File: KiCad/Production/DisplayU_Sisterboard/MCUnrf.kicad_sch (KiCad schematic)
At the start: 1 part, among them U1 nRF52820-CFAA-D-R7

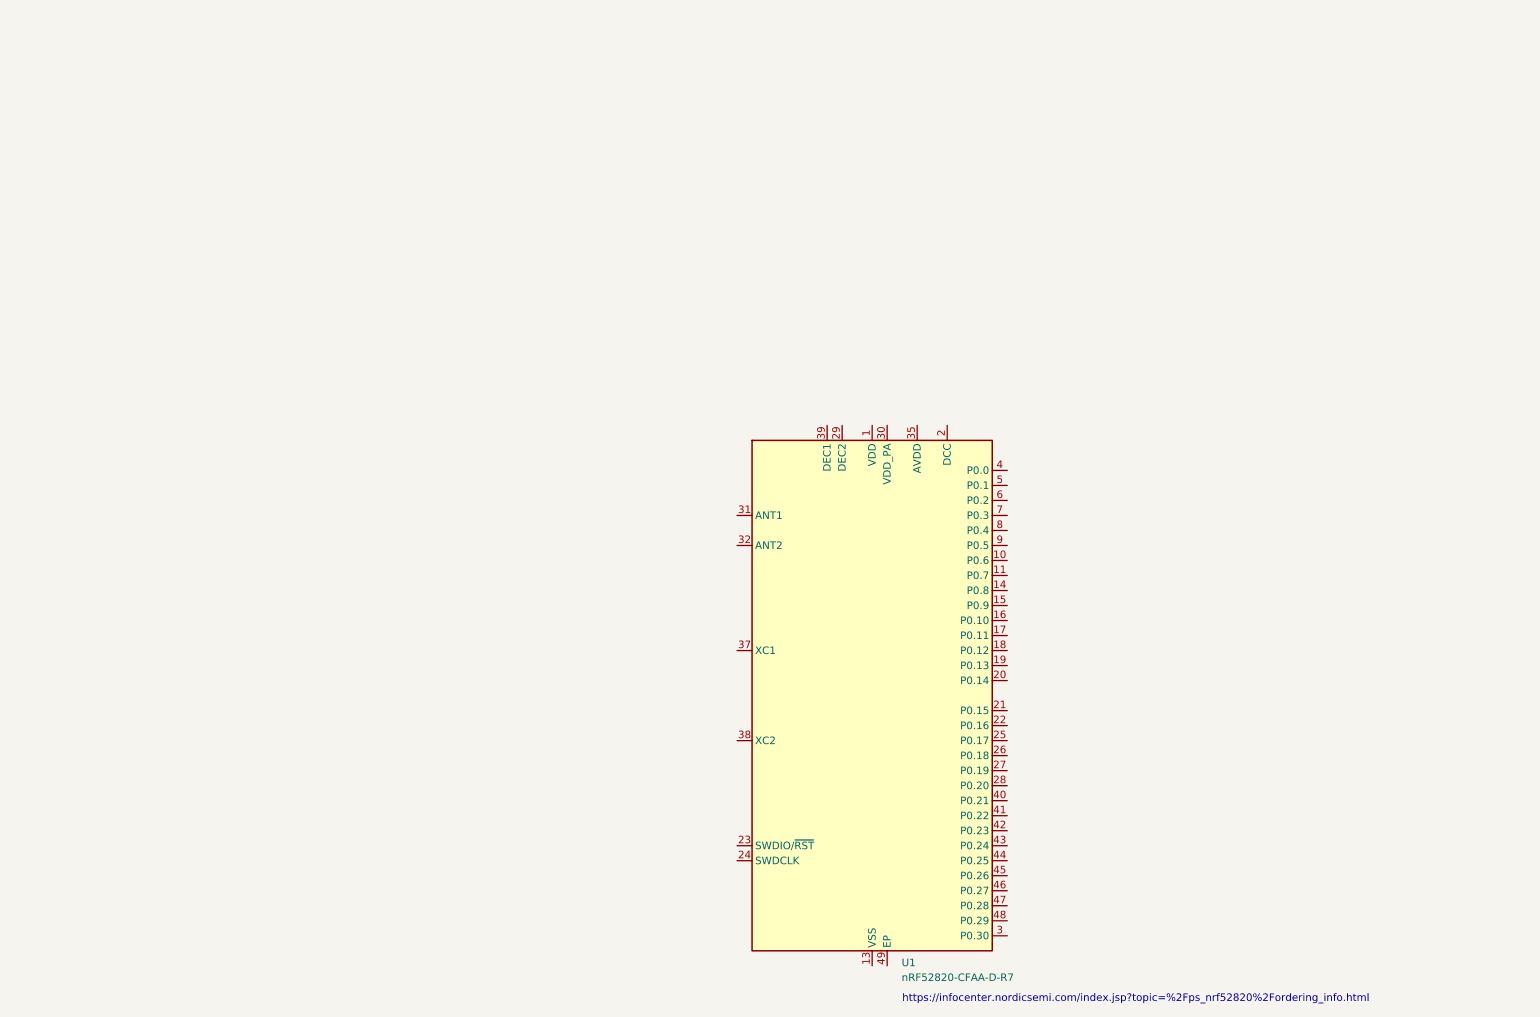
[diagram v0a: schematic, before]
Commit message: Microcontroller Choice
Nordic nRF52820
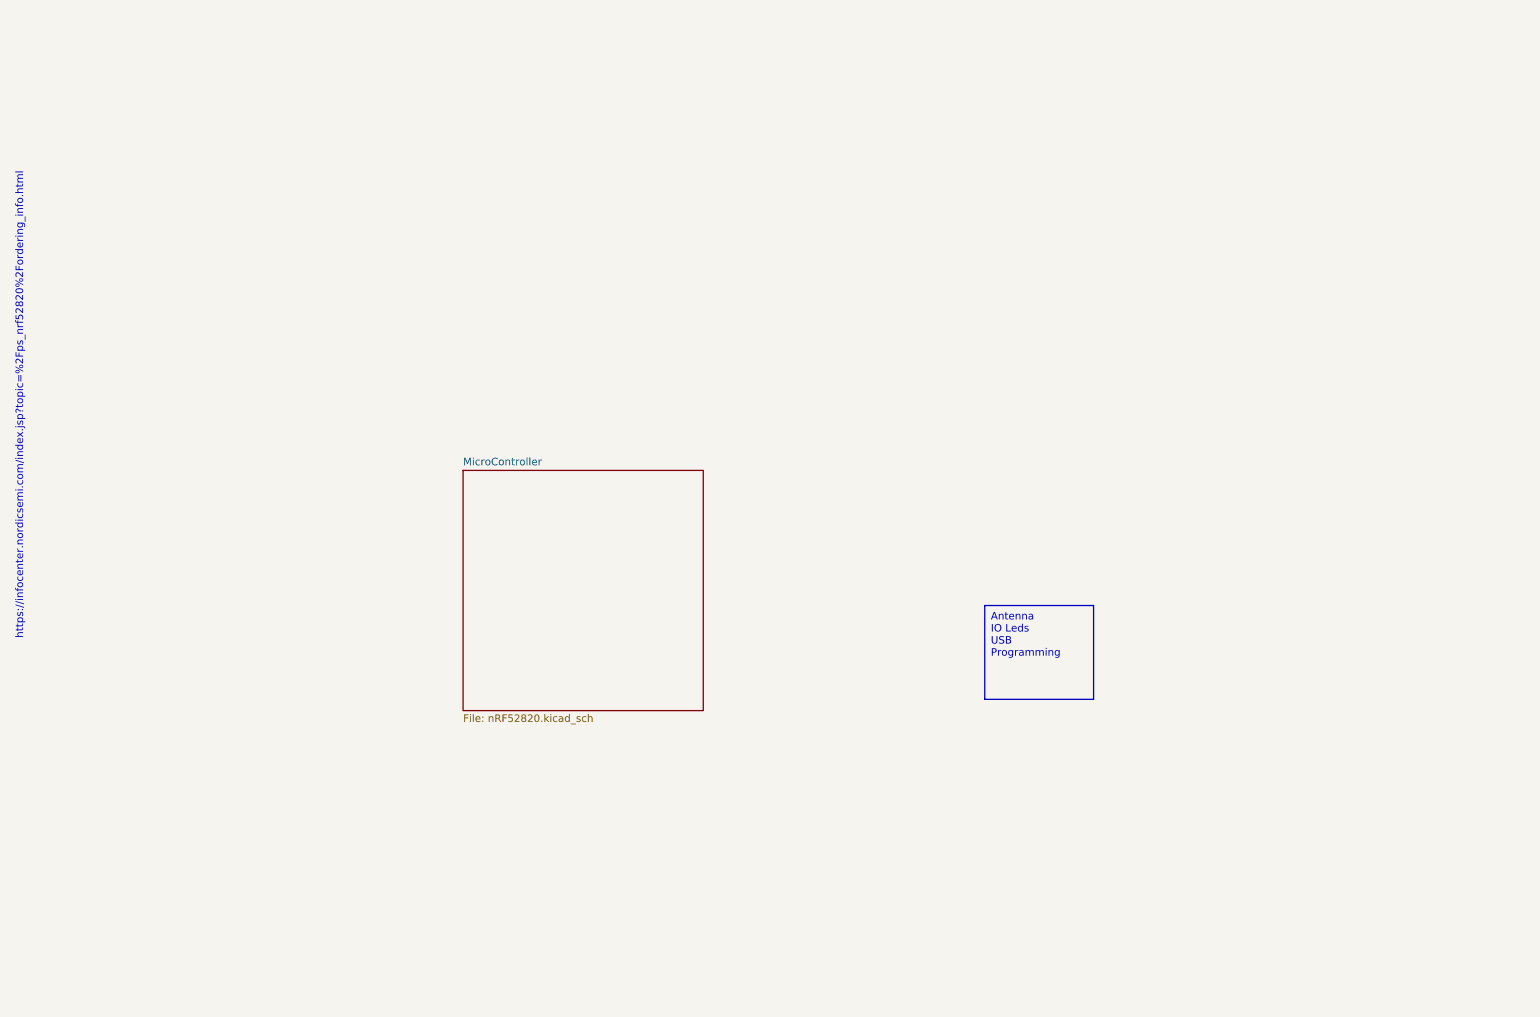
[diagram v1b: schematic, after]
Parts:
- removed U1: nRF52820-CFAA-D-R7, Package_DFN_QFN:QFN-48-1EP_6x6mm_P0.4mm_EP4.6x4.6mm, symbol MCU_Nordic:nRF51x22-QFxx
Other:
- added sheet MicroController (nRF52820.kicad_sch)
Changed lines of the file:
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@@
 (kicad_sch (version 20230121) (generator eeschema)
   (paper "A4")
+  (text_box "Antenna\nIO Leds\nUSB Programming\n\n"
+    (at 171.45 76.835 0) (size 18.415 15.875)
+    (stroke (width 0) (type default))
+    (fill (type none))
+    (effects (font (size 1.27 1.27)) (justify left top))
+  )
   (text "https://infocenter.nordicsemi.com/index.jsp?topic=%2Fps_nrf52820%2Fordering_info.html"
-    (at 157.48 144.145 0)
+    (at 8.89 82.55 90)
     (effects (font (size 1.27 1.27)) (justify left bottom))
   )
-  (symbol (lib_id "MCU_Nordic:nRF51x22-QFxx") (at 152.4 92.075 0) (unit 1)
-    (in_bom yes) (on_board yes) (dnp no) (fields_autoplaced)
-    (property "Reference" "U1" (at 157.3865 137.2696 0)
-      (effects (font (size 1.27 1.27)) (justify left))
+  (sheet (at 83.185 53.975) (size 40.64 40.64) (fields_autoplaced)
+    (stroke (width 0.1524) (type solid))
+    (fill (color 0 0 0 0.0000))
+    (property "Sheetname" "MicroController" (at 83.185 53.2634 0)
+      (effects (font (size 1.27 1.27)) (justify left bottom))
     )
-    (property "Value" "nRF52820-CFAA-D-R7\n" (at 157.3865 139.7748 0)
-      (effects (font (size 1.27 1.27)) (justify left))
+    (property "Sheetfile" "nRF52820.kicad_sch" (at 83.185 95.1996 0)
+      (effects (font (size 1.27 1.27)) (justify left top))
     )
-    (property "Footprint" "Package_DFN_QFN:QFN-48-1EP_6x6mm_P0.4mm_EP4.6x4.6mm" (at 152.4 92.075 0)
-      (effects (font (size 1.27 1.27)) hide)
-    )
-    (property "Datasheet" "http://infocenter.nordicsemi.com/pdf/nRF51822_PS_v3.3.pdf" (at 142.24 94.615 0)
-      (effects (font (size 1.27 1.27)) hide)
-    )
-    (pin "1")
-    (pin "10")
-    (pin "11")
-    (pin "12")
-    (pin "13")
-    (pin "14")
-    (pin "15")
-    (pin "16")
-    (pin "17")
-    (pin "18")
-    (pin "19")
-    (pin "2")
-    (pin "20")
-    (pin "21")
-    (pin "22")
-    (pin "23")
-    (pin "24")
-    (pin "25")
-    (pin "26")
-    (pin "27")
-    (pin "28")
-    (pin "29")
-    (pin "3")
-    (pin "30")
-    (pin "31")
-    (pin "32")
-    (pin "33")
-    (pin "34")
-    (pin "35")
-    (pin "36")
-    (pin "37")
-    (pin "38")
-    (pin "39")
-    (pin "4")
-    (pin "40")
-    (pin "41")
-    (pin "42")
-    (pin "43")
-    (pin "44")
-    (pin "45")
-    (pin "46")
-    (pin "47")
-    (pin "48")
-    (pin "49")
-    (pin "5")
-    (pin "6")
-    (pin "7")
-    (pin "8")
-    (pin "9")
     (instances
       (project "DisplayU_Sisterboard"
-        (path "/19c7c935-33c8-4c59-9a5d-d605e15c31a3"
-          (reference "U1") (unit 1)
-        )
-        (path "/19c7c935-33c8-4c59-9a5d-d605e15c31a3/25a7bd83-bec9-4f3f-8272-59937481b0db"
-          (reference "U1") (unit 1)
-        )
+        (path "/19c7c935-33c8-4c59-9a5d-d605e15c31a3/25a7bd83-bec9-4f3f-8272-59937481b0db" (page "5"))
       )
     )
